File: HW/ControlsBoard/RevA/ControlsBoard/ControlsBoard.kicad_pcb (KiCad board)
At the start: 2 copper layers, 38.7 x 48.3 mm, 16 parts, among them J1 Conn_02x06_Odd_Even, SW1 Rotary_Encoder_Switch, U1 Tactile_Switch_SPST-NO, U2 Tactile_Switch_SPST-NO, U3 Tactile_Switch_SPST-NO, U4 Tactile_Switch_SPST-NO

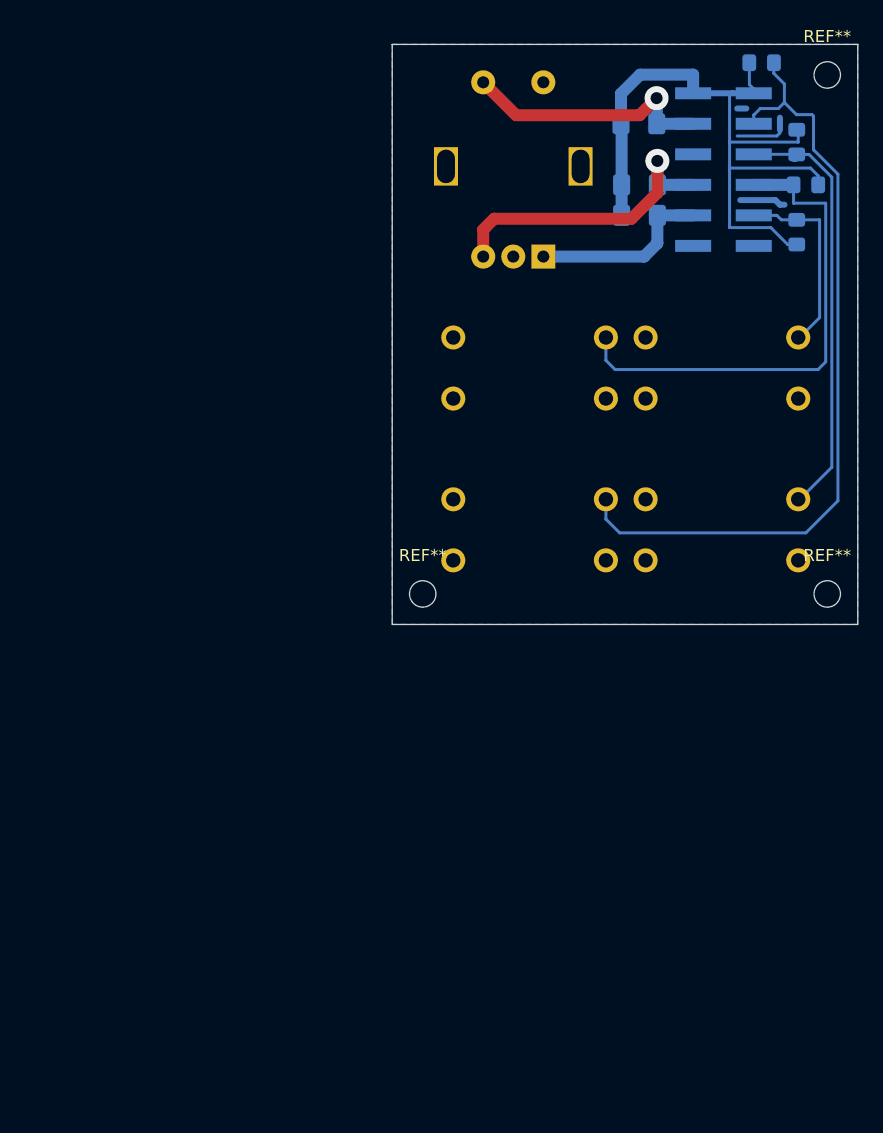
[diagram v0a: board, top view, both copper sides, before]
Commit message: Added Revb designs for I/O and control panels
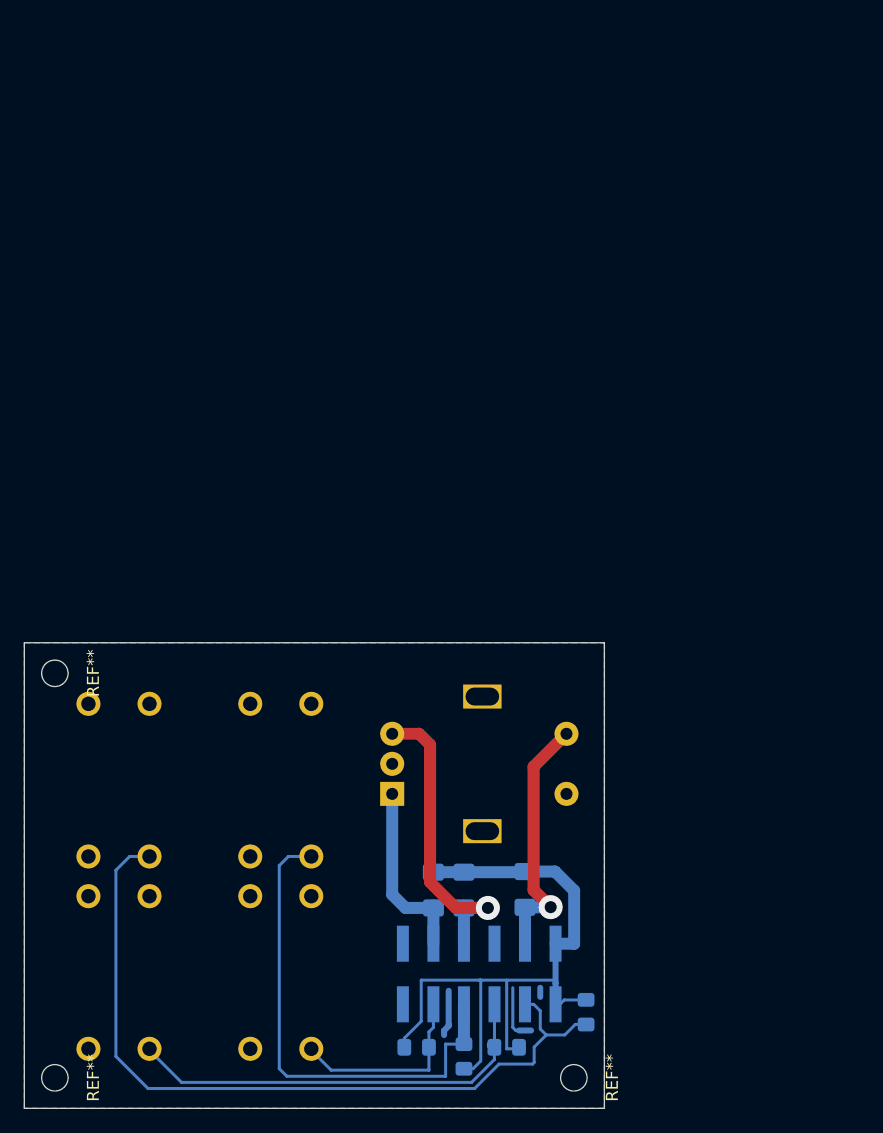
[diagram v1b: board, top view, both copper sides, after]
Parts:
- moved REF** 86.1 mm to (130.7, 140.4), turned to 270 degrees
- moved R1 80.3 mm to (131.8, 134.9), turned to 270 degrees
- moved R2 79.1 mm to (125.2, 137.9), turned to 180 degrees
- moved R3 77.9 mm to (121.6, 138.6), turned to 90 degrees
- moved REF** 75.8 mm to (87.6, 140.4), turned to 270 degrees
- moved R4 74.8 mm to (117.7, 137.9), turned to 0 degrees
- moved J1 69.9 mm to (122.9, 131.8), turned to 90 degrees
- moved R6 64.4 mm to (126.7, 124.7), turned to 270 degrees
- moved U4 62.3 mm to (106.4, 131.6), turned to 90 degrees
- moved U2 62.2 mm to (92.9, 131.6), turned to 90 degrees
- moved R7 60.5 mm to (121.6, 124.8), turned to 270 degrees
- moved R5 58.7 mm to (119.1, 124.8), turned to 270 degrees
- moved SW1 46.4 mm to (115.6, 116.8), turned to 0 degrees
- moved U3 40.1 mm to (106.4, 115.6), turned to 90 degrees
- moved U1 40.0 mm to (92.9, 115.6), turned to 90 degrees
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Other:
- board size 38.7 x 48.3 mm -> 48.3 x 38.7 mm
